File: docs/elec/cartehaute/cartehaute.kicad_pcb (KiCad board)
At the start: 2 copper layers, 51.7 x 40.3 mm, 14 parts, among them P1 Servo, P10 Analog, P11 AN2, P12 12V, P13 19V, P14 19/12V, P2 Yeux, P3 LED, P4 HUB, P5 Servo2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

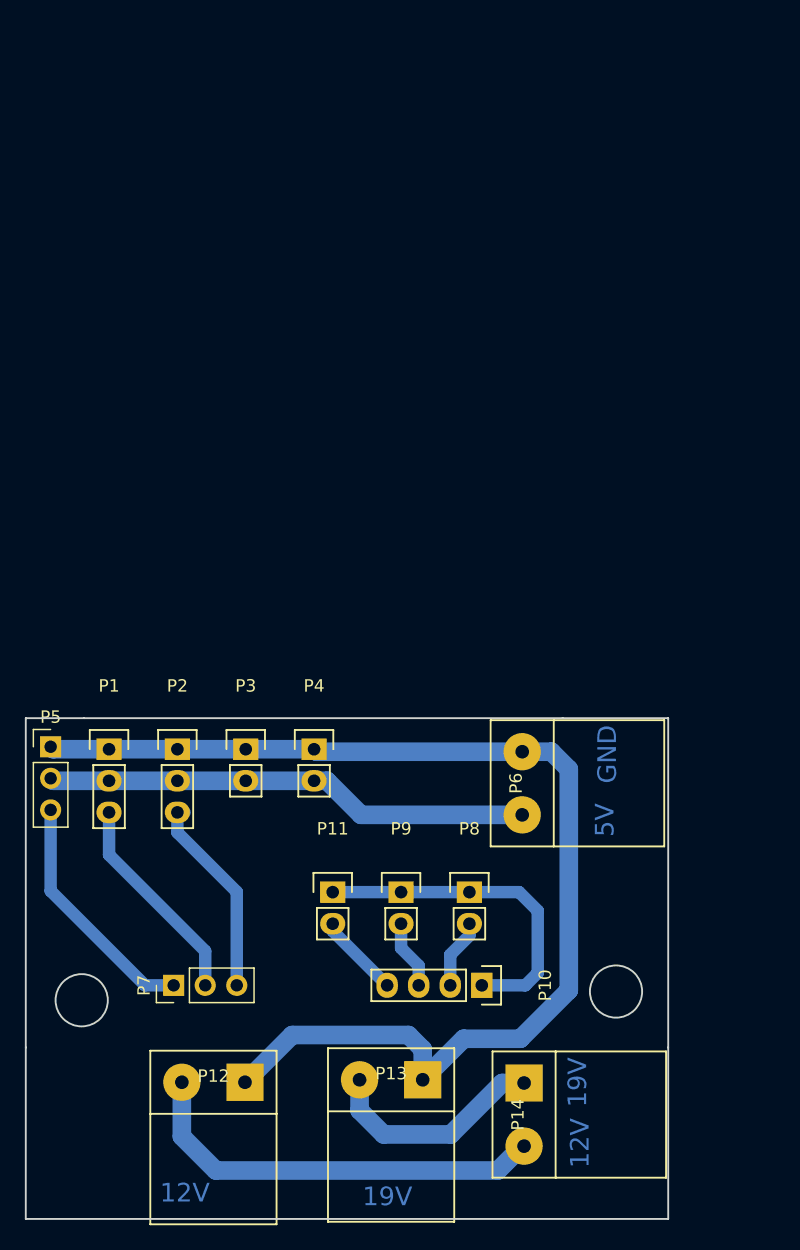
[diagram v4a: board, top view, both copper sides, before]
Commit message: Simplify the top board
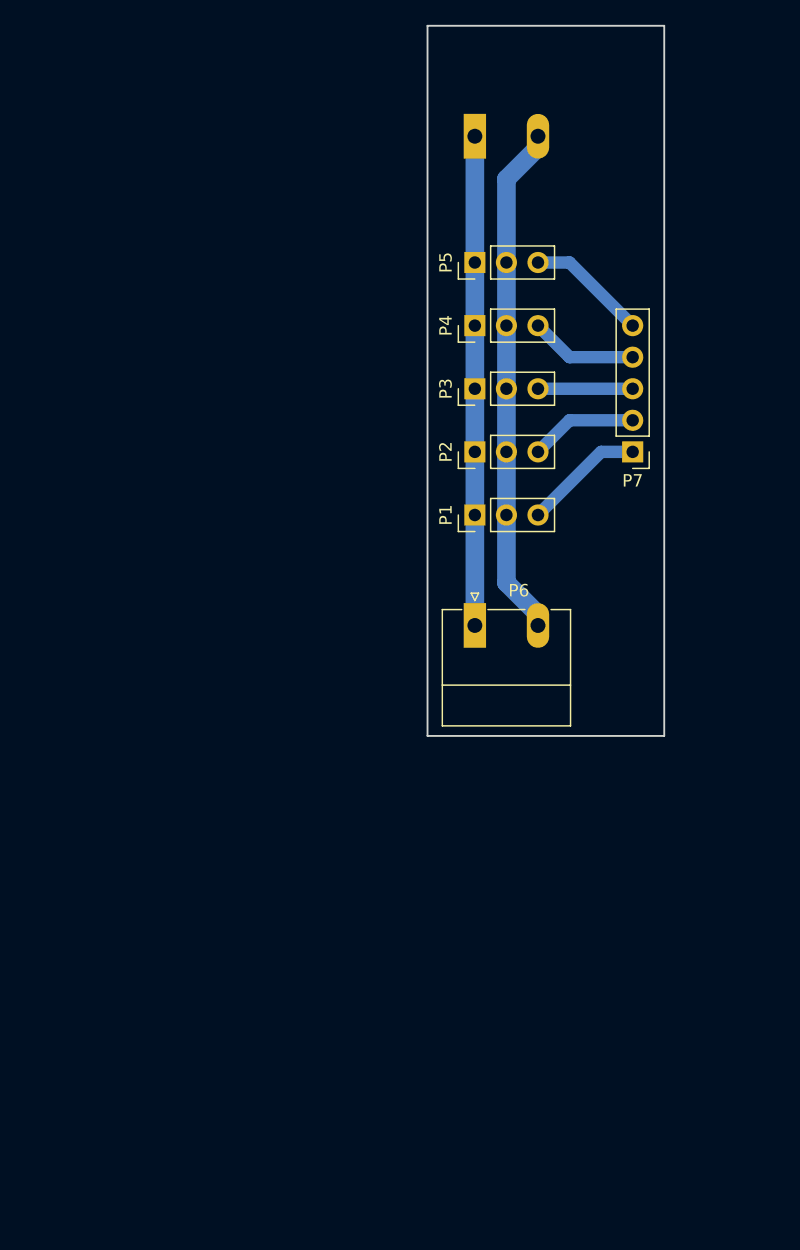
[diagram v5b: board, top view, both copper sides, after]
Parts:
- removed P10: Analog, Pin_Headers:Pin_Header_Straight_1x04
- removed P11: AN2, Pin_Headers:Pin_Header_Straight_1x02
- removed P12: 12V, robair:Bornier5mm
- removed P13: 19V, robair:Bornier5mm
- removed P14: 19/12V, robair:Bornier5mm
- removed P9: AN1, Pin_Headers:Pin_Header_Straight_1x02
- P1: value Servo -> D1; footprint Pin_Headers:Pin_Header_Straight_1x03 -> Pin_Headers:Pin_Header_Straight_1x03_Pitch2.54mm
- P2: value Yeux -> D2; footprint Pin_Headers:Pin_Header_Straight_1x03 -> Pin_Headers:Pin_Header_Straight_1x03_Pitch2.54mm
- P3: value LED -> D3; footprint Pin_Headers:Pin_Header_Straight_1x02 -> Pin_Headers:Pin_Header_Straight_1x03_Pitch2.54mm
- P4: value HUB -> D4; footprint Pin_Headers:Pin_Header_Straight_1x02 -> Pin_Headers:Pin_Header_Straight_1x03_Pitch2.54mm
- P5: value Servo2 -> D5
- P6: value 5V -> CONN_01X02; footprint robair:Bornier5mm -> Connectors_Phoenix:PhoenixContact_MC-G_02x5.08mm_Angled
- P7: value data -> CONN_01X05; footprint Pin_Headers:Pin_Header_Straight_1x03_Pitch2.54mm -> Pin_Headers:Pin_Header_Straight_1x05_Pitch2.54mm
- P8: value ARU -> CONN_01X02; footprint Pin_Headers:Pin_Header_Straight_1x02 -> Connectors_Phoenix:PhoenixContact_MC-G_02x5.08mm_Angled; moved to B.Cu
- moved P8 60.8 mm to (154.9, 26.7)
- moved P7 56.6 mm to (167.6, 52.1), turned to 180 degrees
- moved P5 51.8 mm to (154.9, 36.8), turned to 90 degrees
- moved P4 36.5 mm to (154.9, 41.9), turned to 90 degrees
- moved P1 35.0 mm to (154.9, 57.1), turned to 90 degrees
- moved P3 34.4 mm to (154.9, 47.0), turned to 90 degrees
- moved P2 33.8 mm to (154.9, 52.1), turned to 90 degrees
- moved P6 13.3 mm to (154.9, 66.0), turned to 0 degrees
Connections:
- P7 pad 1: Net-(P5-Pad3) -> Net-(P1-Pad3)
- P7 pad 2: Net-(P1-Pad3) -> Net-(P2-Pad3)
- P7 pad 3: Net-(P2-Pad3) -> Net-(P3-Pad3)
- P8 pad 1: Net-(P10-Pad1) -> /GND
- P8 pad 2: Net-(P10-Pad2) -> /5V
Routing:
- net /GND: track 93.8 -> 39.4 mm
- net Net-(P12-Pad2): track 33.8 -> 0.00 mm
- net Net-(P10-Pad1): track 27.0 -> 0.00 mm
- net Net-(P13-Pad2): track 18.2 -> 0.00 mm
- net Net-(P5-Pad3): track 19.6 -> 9.72 mm
- net Net-(P4-Pad3): track 0.00 -> 8.67 mm
- net Net-(P2-Pad3): track 16.5 -> 8.67 mm
- net Net-(P3-Pad3): track 0.00 -> 7.62 mm
- net Net-(P1-Pad3): track 17.1 -> 9.72 mm
- net Net-(P10-Pad4): track 6.77 -> 0.00 mm
- net Net-(P10-Pad2): track 5.60 -> 0.00 mm
- net Net-(P10-Pad3): track 5.55 -> 0.00 mm
- net /5V: track 39.2 -> 41.5 mm
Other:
- board size 51.7 x 40.3 mm -> 19.1 x 57.2 mm
- board text removed: "12V"
- board text removed: "19V"
- board text removed: "5V"
- board text removed: "GND"
